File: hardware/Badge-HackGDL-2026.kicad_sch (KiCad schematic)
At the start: 0 parts

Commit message: feat(Hw):Update_Schematic_And_BOM
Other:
- sheet Cam ports: added CSI_SCK, CSI_SDA, MCSI_CKN, MCSI_CKP, MCSI_D0N, MCSI_D0P, MCSI_D1N, MCSI_D1P, MCSI_MCLK, MCSI_RST, v_3v3; removed none
- sheet MCU ports: added CSI_SCK, CSI_SDA, MCSI_CKN, MCSI_CKP, MCSI_D0N, MCSI_D0P, MCSI_D1N, MCSI_D1P, MCSI_MCLK, MCSI_RST; removed none
- sheet Otros ports: added none; removed DIN_IR, PB1, PB2

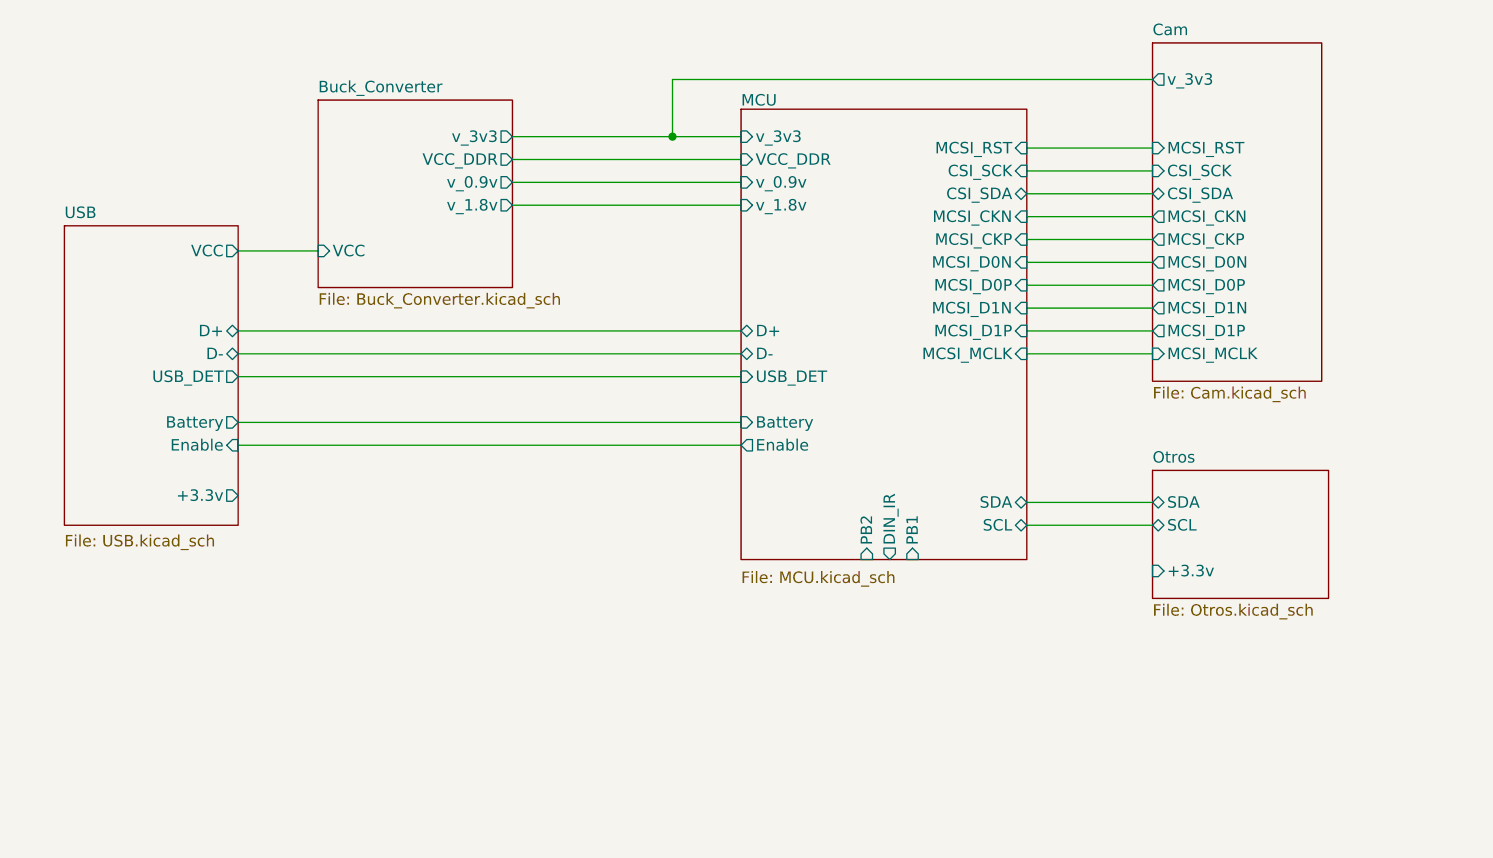
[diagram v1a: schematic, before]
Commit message: feat(Hw):Update_Schematic_And_Floorplan
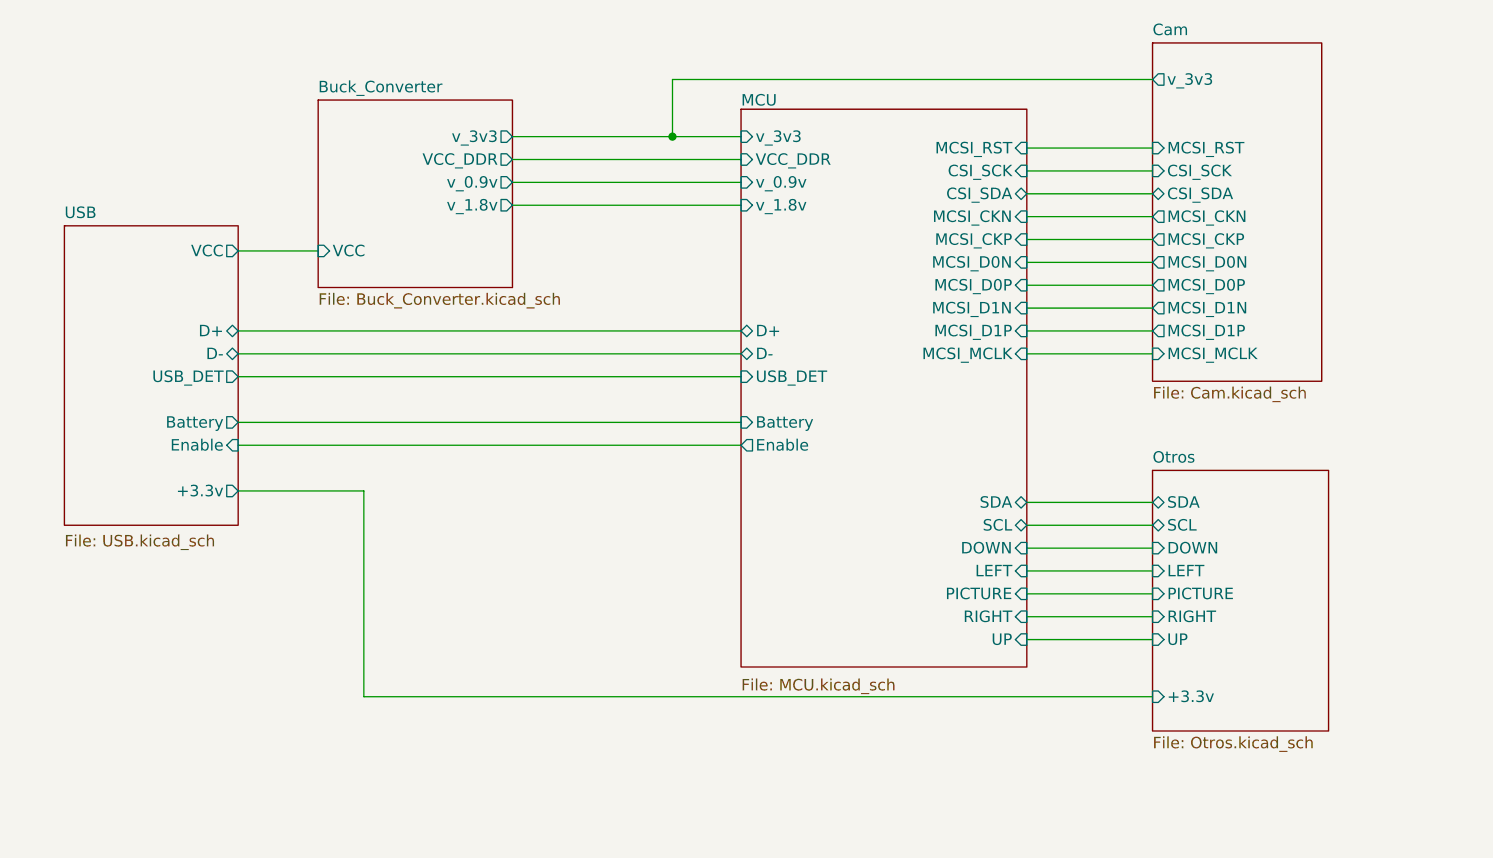
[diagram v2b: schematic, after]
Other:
- sheet MCU ports: added DOWN, LEFT, PICTURE, RIGHT, UP; removed DIN_IR, PB1, PB2
- sheet Otros ports: added DOWN, LEFT, PICTURE, RIGHT, UP; removed none
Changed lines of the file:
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@@
+	(wire
+		(pts
+			(xy 99.06 111.76) (xy 113.03 111.76)
+		)
+		(stroke
+			(width 0)
+			(type default)
+		)
+	)
+	(wire
+		(pts
+			(xy 186.69 118.11) (xy 200.66 118.11)
+		)
+		(stroke
+			(width 0)
+			(type default)
+		)
+	)
 	(wire
 		(pts
@@
 	(wire
 		(pts
+			(xy 186.69 120.65) (xy 200.66 120.65)
+		)
+		(stroke
+			(width 0)
+			(type default)
+		)
+	)
+	(wire
+		(pts
 			(xy 99.06 96.52) (xy 154.94 96.52)
 		)
@@
 	(wire
 		(pts
+			(xy 186.69 125.73) (xy 200.66 125.73)
+		)
+		(stroke
+			(width 0)
+			(type default)
+		)
+	)
+	(wire
+		(pts
 			(xy 186.69 73.66) (xy 200.66 73.66)
 		)
@@
 	(wire
 		(pts
+			(xy 186.69 123.19) (xy 200.66 123.19)
+		)
+		(stroke
+			(width 0)
+			(type default)
+		)
+	)
+	(wire
+		(pts
+			(xy 113.03 111.76) (xy 113.03 134.62)
+		)
+		(stroke
+			(width 0)
+			(type default)
+		)
+	)
+	(wire
+		(pts
 			(xy 147.32 72.39) (xy 147.32 66.04)
 		)
@@
 	(wire
 		(pts
+			(xy 186.69 128.27) (xy 200.66 128.27)
+		)
+		(stroke
+			(width 0)
+			(type default)
+		)
+	)
+	(wire
+		(pts
 			(xy 129.54 74.93) (xy 154.94 74.93)
+		)
+		(stroke
+			(width 0)
+			(type default)
+		)
+	)
+	(wire
+		(pts
+			(xy 113.03 134.62) (xy 200.66 134.62)
 		)
 		(stroke
@@
 	(sheet
 		(at 200.66 109.474)
-		(size 19.558 14.224)
+		(size 19.558 28.956)
 		(exclude_from_sim no)
 		(in_bom yes)
@@
 		)
 		(property "Sheetfile" "Otros.kicad_sch"
-			(at 200.66 124.2826 0)
+			(at 200.66 139.0146 0)
 			(effects
 				(font
@@
 		)
 		(pin "+3.3v" input
+			(at 200.66 134.62 180)
+			(effects
+				(font
+					(size 1.27 1.27)
+				)
+				(justify left)
+			)
+		)
+		(pin "DOWN" input
+			(at 200.66 118.11 180)
+			(effects
+				(font
+					(size 1.27 1.27)
+				)
+				(justify left)
+			)
+		)
+		(pin "LEFT" input
 			(at 200.66 120.65 180)
+			(effects
+				(font
+					(size 1.27 1.27)
+				)
+				(justify left)
+			)
+		)
+		(pin "PICTURE" input
+			(at 200.66 123.19 180)
+			(effects
+				(font
+					(size 1.27 1.27)
+				)
+				(justify left)
+			)
+		)
+		(pin "RIGHT" input
+			(at 200.66 125.73 180)
+			(effects
+				(font
+					(size 1.27 1.27)
+				)
+				(justify left)
+			)
+		)
+		(pin "UP" input
+			(at 200.66 128.27 180)
 			(effects
 				(font
@@
 		)
 		(pin "+3.3v" output
-			(at 99.06 112.268 0)
+			(at 99.06 111.76 0)
 			(effects
 				(font
@@
 	(sheet
 		(at 154.94 69.342)
-		(size 31.75 50.038)
+		(size 31.75 61.976)
 		(exclude_from_sim no)
 		(in_bom yes)
@@
 		)
 		(property "Sheetfile" "MCU.kicad_sch"
-			(at 154.94 120.65 0)
+			(at 154.94 132.588 0)
 			(effects
 				(font
@@
 			)
 		)
-		(pin "DIN_IR" output
-			(at 171.45 119.38 270)
-			(effects
-				(font
-					(size 1.27 1.27)
-				)
-				(justify left)
-			)
-		)
 		(pin "Enable" output
 			(at 154.94 106.68 180)
@@
 			)
 		)
-		(pin "PB1" input
-			(at 173.99 119.38 270)
-			(effects
-				(font
-					(size 1.27 1.27)
-				)
-				(justify left)
-			)
-		)
-		(pin "PB2" input
-			(at 168.91 119.38 270)
-			(effects
-				(font
-					(size 1.27 1.27)
-				)
-				(justify left)
-			)
-		)
 		(pin "SCL" bidirectional
 			(at 186.69 115.57 0)
@@
 			)
 		)
+		(pin "DOWN" input
+			(at 186.69 118.11 0)
+			(effects
+				(font
+					(size 1.27 1.27)
+				)
+				(justify right)
+			)
+		)
+		(pin "LEFT" input
+			(at 186.69 120.65 0)
+			(effects
+				(font
+					(size 1.27 1.27)
+				)
+				(justify right)
+			)
+		)
+		(pin "PICTURE" input
+			(at 186.69 123.19 0)
+			(effects
+				(font
+					(size 1.27 1.27)
+				)
+				(justify right)
+			)
+		)
+		(pin "RIGHT" input
+			(at 186.69 125.73 0)
+			(effects
+				(font
+					(size 1.27 1.27)
+				)
+				(justify right)
+			)
+		)
+		(pin "UP" input
+			(at 186.69 128.27 0)
+			(effects
+				(font
+					(size 1.27 1.27)
+				)
+				(justify right)
+			)
+		)

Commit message: feat(Hw):Update_Floorplan_And_Route
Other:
- sheet MCU ports: added DIN_IR; removed none
- sheet Otros ports: added DIN_IR; removed none
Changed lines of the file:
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@@
 	(wire
 		(pts
-			(xy 113.03 111.76) (xy 113.03 134.62)
+			(xy 113.03 111.76) (xy 113.03 138.43)
 		)
 		(stroke
@@
 	(wire
 		(pts
+			(xy 186.69 130.81) (xy 200.66 130.81)
+		)
+		(stroke
+			(width 0)
+			(type default)
+		)
+	)
+	(wire
+		(pts
 			(xy 186.69 88.9) (xy 200.66 88.9)
 		)
@@
 	(wire
 		(pts
-			(xy 113.03 134.62) (xy 200.66 134.62)
+			(xy 113.03 138.43) (xy 200.66 138.43)
 		)
 		(stroke
@@
 	(sheet
 		(at 200.66 109.474)
-		(size 19.558 28.956)
+		(size 19.558 32.766)
 		(exclude_from_sim no)
 		(in_bom yes)
@@
 		)
 		(property "Sheetfile" "Otros.kicad_sch"
-			(at 200.66 139.0146 0)
+			(at 200.66 142.8246 0)
 			(effects
 				(font
@@
 		)
 		(pin "+3.3v" input
-			(at 200.66 134.62 180)
+			(at 200.66 138.43 180)
 			(effects
 				(font
@@
 		(pin "UP" input
 			(at 200.66 128.27 180)
+			(effects
+				(font
+					(size 1.27 1.27)
+				)
+				(justify left)
+			)
+		)
+		(pin "DIN_IR" input
+			(at 200.66 130.81 180)
 			(effects
 				(font
@@
 	(sheet
 		(at 154.94 69.342)
-		(size 31.75 61.976)
+		(size 31.75 65.278)
 		(exclude_from_sim no)
 		(in_bom yes)
@@
 		)
 		(property "Sheetfile" "MCU.kicad_sch"
-			(at 154.94 132.588 0)
+			(at 154.94 135.382 0)
 			(effects
 				(font
@@
 			(effects
 				(font
+					(size 1.27 1.27)
+				)
+				(justify right)
+			)
+		)
+		(pin "DIN_IR" output
+			(at 186.69 130.81 0)
+			(effects
+				(font

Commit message: feat(Hw):Update_Schematic_And_Route
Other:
- sheet Cam ports: added +3.3v; removed v_3v3
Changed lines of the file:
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@@
 	(paper "A4")
 	(junction
-		(at 147.32 72.39)
+		(at 193.04 138.43)
 		(diameter 0)
-		(color 255 59 54 1)
+		(color 255 38 39 1)
 	)
 	(wire
@@
 	(wire
 		(pts
-			(xy 129.54 72.39) (xy 147.32 72.39)
+			(xy 129.54 72.39) (xy 154.94 72.39)
 		)
 		(stroke
@@
 			(width 0)
 			(type default)
+			(color 255 38 39 1)
 		)
 	)
@@
 	(wire
 		(pts
-			(xy 147.32 66.04) (xy 200.66 66.04)
-		)
-		(stroke
-			(width 0)
-			(type default)
-			(color 255 59 54 1)
-		)
-	)
-	(wire
-		(pts
 			(xy 186.69 78.74) (xy 200.66 78.74)
 		)
@@
 	(wire
 		(pts
+			(xy 200.66 99.06) (xy 193.04 99.06)
+		)
+		(stroke
+			(width 0)
+			(type default)
+			(color 255 38 39 1)
+		)
+	)
+	(wire
+		(pts
 			(xy 186.69 73.66) (xy 200.66 73.66)
 		)
@@
 	(wire
 		(pts
+			(xy 193.04 99.06) (xy 193.04 138.43)
+		)
+		(stroke
+			(width 0)
+			(type default)
+			(color 255 38 39 1)
+		)
+	)
+	(wire
+		(pts
 			(xy 186.69 123.19) (xy 200.66 123.19)
 		)
@@
 			(width 0)
 			(type default)
-		)
-	)
-	(wire
-		(pts
-			(xy 147.32 72.39) (xy 147.32 66.04)
-		)
-		(stroke
-			(width 0)
-			(type default)
-			(color 255 59 54 1)
+			(color 255 38 39 1)
 		)
 	)
@@
 	(wire
 		(pts
-			(xy 147.32 72.39) (xy 154.94 72.39)
-		)
-		(stroke
-			(width 0)
-			(type default)
-			(color 255 59 54 1)
-		)
-	)
-	(wire
-		(pts
 			(xy 186.69 81.28) (xy 200.66 81.28)
 		)
@@
 	(wire
 		(pts
+			(xy 193.04 138.43) (xy 200.66 138.43)
+		)
+		(stroke
+			(width 0)
+			(type default)
+			(color 255 38 39 1)
+		)
+	)
+	(wire
+		(pts
 			(xy 129.54 74.93) (xy 154.94 74.93)
 		)
@@
 	(wire
 		(pts
-			(xy 113.03 138.43) (xy 200.66 138.43)
-		)
-		(stroke
-			(width 0)
-			(type default)
+			(xy 113.03 138.43) (xy 193.04 138.43)
+		)
+		(stroke
+			(width 0)
+			(type default)
+			(color 255 38 39 1)
 		)
 	)
@@
 	)
 	(sheet
-		(at 200.66 61.976)
-		(size 18.796 37.592)
+		(at 200.66 71.12)
+		(size 18.796 30.48)
 		(exclude_from_sim no)
 		(in_bom yes)
@@
 		)
 		(property "Sheetname" "Cam"
-			(at 200.66 61.2644 0)
+			(at 200.66 70.4084 0)
 			(effects
 				(font
@@
 		)
 		(property "Sheetfile" "Cam.kicad_sch"
-			(at 200.66 100.1526 0)
+			(at 200.66 102.1846 0)
 			(effects
 				(font
@@
 			)
 		)
-		(pin "v_3v3" output
-			(at 200.66 66.04 180)
-			(effects
-				(font
+		(pin "+3.3v" input
+			(at 200.66 99.06 180)
+			(effects
+				(font

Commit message: feat(Hw):Update_3Dmodels_And_Rear_Board
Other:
- company: (none) -> Electronic Cats
- title: (none) -> Badge-HackGDL-2026
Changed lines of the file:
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@@
 	(generator_version "9.0")
 	(paper "A4")
+	(title_block
+		(title "Badge-HackGDL-2026")
+		(date "2026-01-15")
+		(rev "v1.0")
+		(company "Electronic Cats")
+		(comment 1 "Lizeth Gallegos Martínez")
+	)
 	(junction
 		(at 193.04 138.43)

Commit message: feat(Hw):Update_Shematic_And_PCB
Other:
- added sheet Support pins (Support pins.kicad_sch)
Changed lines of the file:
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@@
+	)
+	(sheet
+		(at 120.65 113.03)
+		(size 22.86 17.78)
+		(exclude_from_sim no)
+		(in_bom yes)
+		(on_board yes)
+		(dnp no)
+		(fields_autoplaced yes)
+		(stroke
+			(width 0.1524)
+			(type solid)
+		)
+		(fill
+			(color 0 0 0 0.0000)
+		)
+		(property "Sheetname" "Support pins"
+			(at 120.65 112.3184 0)
+			(effects
+				(font
+					(size 1.27 1.27)
+				)
+				(justify left bottom)
+			)
+		)
+		(property "Sheetfile" "Support pins.kicad_sch"
+			(at 120.65 131.3946 0)
+			(effects
+				(font
+					(size 1.27 1.27)
+				)
+				(justify left top)
+			)
+		)
+		(instances
+			(project "Badge-HackGDL-2026"
+				(path "/aee06ce3-1da5-4230-bf8f-9d1068f7ddd5"
+					(page "7")
+				)
+			)
+		)
 	)
 	(sheet
